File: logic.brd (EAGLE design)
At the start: 37.4 x 32.5 mm, 8 parts, among them CON1 PINHEAD_1X10-2, CON2 PINHEAD_1X10-2, CON3 PINHEAD_1X06-2, CON4 PINHEAD_1X02-2, CON5 PINHEAD_1X02-2, CON6 PINHEAD_1X02-2

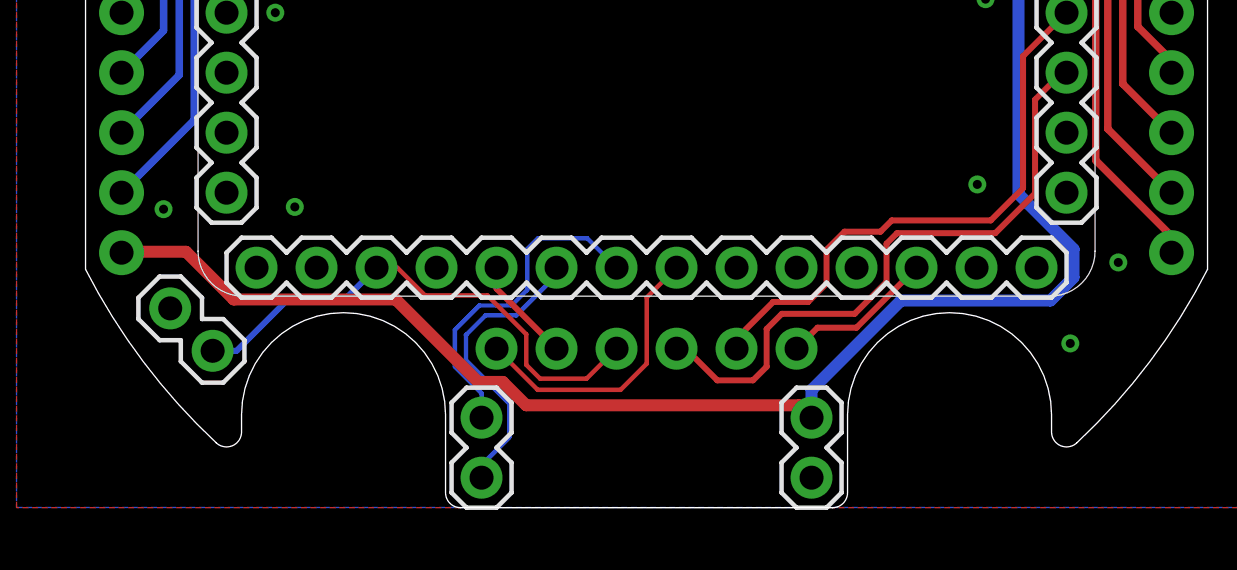
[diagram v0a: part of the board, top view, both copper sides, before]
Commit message: Routing is complete again. Now with BEC output
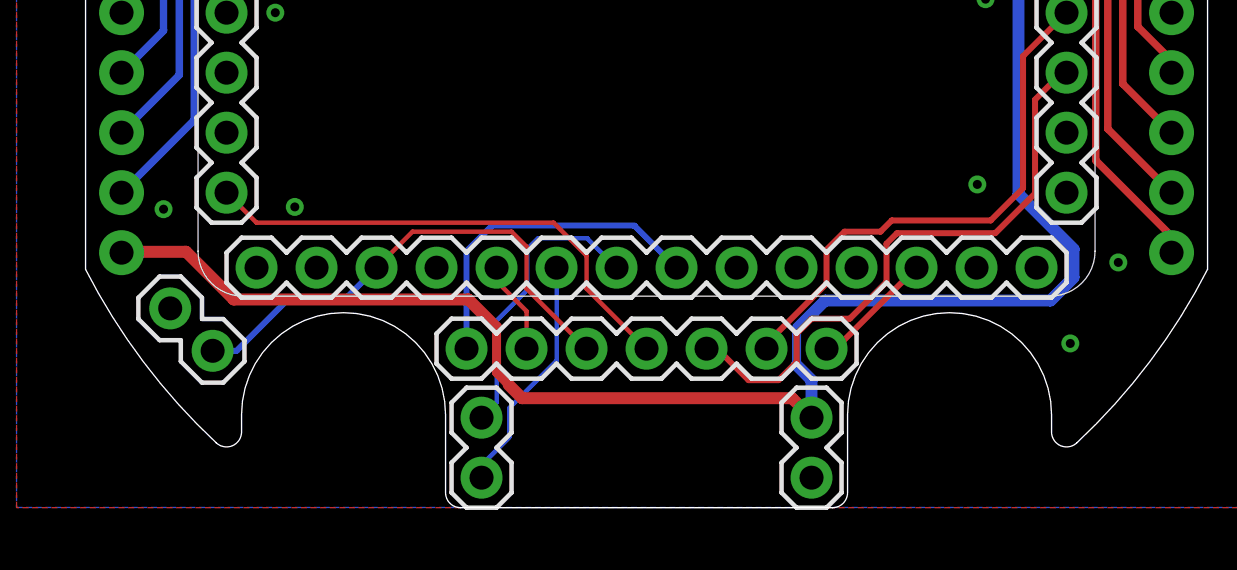
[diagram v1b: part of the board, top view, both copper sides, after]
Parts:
- removed CON3: PINHEAD_1X06-2, pinhead:1X06-PTH-2
- added CON7: PINHEAD_1X07-2, pinhead:1X07-PTH-2
- added U$2: (no value), logo:OSHW-10.5X11.5
- moved U$1 6.70 mm to (6.22, 4.55)
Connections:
- new net BEC_ENABLE: CON7.4, MODULE2.24
- net ADJ: now also CON7.2; no longer CON3.2
- net BLUE: now also CON7.1; no longer CON3.1
- net CAN1_LED: now also CON7.7; no longer CON3.6
- net CAN1_RX: now also CON7.5; no longer CON3.4
- net CAN1_TX: now also CON7.6; no longer CON3.5
- net GPIO1: now also CON7.3; no longer CON3.3
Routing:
- net BEC_ENABLE: track 0.00 -> 16.8 mm
- net VDD_5V: track 62.4 -> 65.2 mm
- net BLUE: track 9.55 -> 11.2 mm
- net RED: track 9.83 -> 8.28 mm
- net GREEN: track 11.1 -> 9.78 mm
- net CAN1_RX: track 21.0 -> 19.8 mm
- net CAN1_TX: track 19.1 -> 18.0 mm
- net CAN1_LED: track 5.12 -> 4.12 mm
- net GPIO1: track 17.2 -> 16.5 mm

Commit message: bloody connectors
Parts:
- moved CON1 0.30 mm to (17.2, 0.00)
- moved CON2 0.30 mm to (-17.2, 0.00)
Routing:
- net PHASE_B_GATE_HIGH: track 30.6 -> 28.5 mm, vias 0 -> 1
- net VDD_5V: track 65.2 -> 67.0 mm
